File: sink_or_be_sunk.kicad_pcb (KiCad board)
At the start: 2 copper layers, 85.6 x 78.9 mm, 77 parts, among them J1 Grid_Conn_LED, J10 Grid_Conn, J11 Grid_Conn, J12 Grid_Conn, J13 Grid_Conn, J14 Grid_Conn, J15 Grid_Conn, J16 Grid_Conn, J18 Keypad_Conn, J19 Display_Conn, J2 Grid_Conn, J20 JTAG_Conn, J21 Debug_Conn, J22 Battery_Conn, J23 USB_B_Micro, J3 Grid_Conn, J4 Grid_Conn, J5 Grid_Conn, J6 Grid_Conn, J7 Grid_Conn, J8 Grid_Conn, J9 Grid_Conn, M1 Motor_DC, Q1 IRL530, Q2 Q_PMOS_DGS, Q3 2N3704, Q4 2N3704, SW1 SW_DPST, SW2 Reset_SW, U1 SN74HC151N, U2 SwitchingRegulator, U3 MCP73831-2-OT, U4 MCP608, U5 ESP32-WROOM-32, U6 CY7C65213A-28PVXI

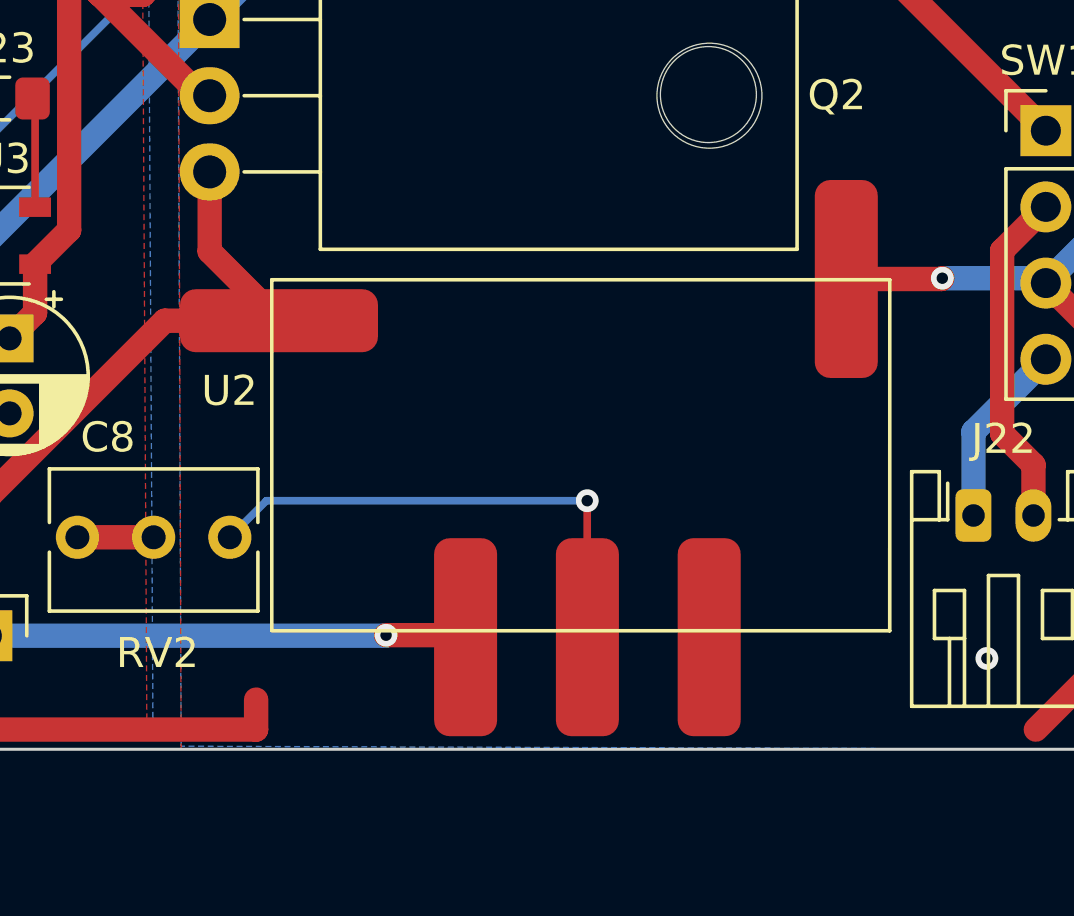
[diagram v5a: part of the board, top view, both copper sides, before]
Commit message: before switching pmos
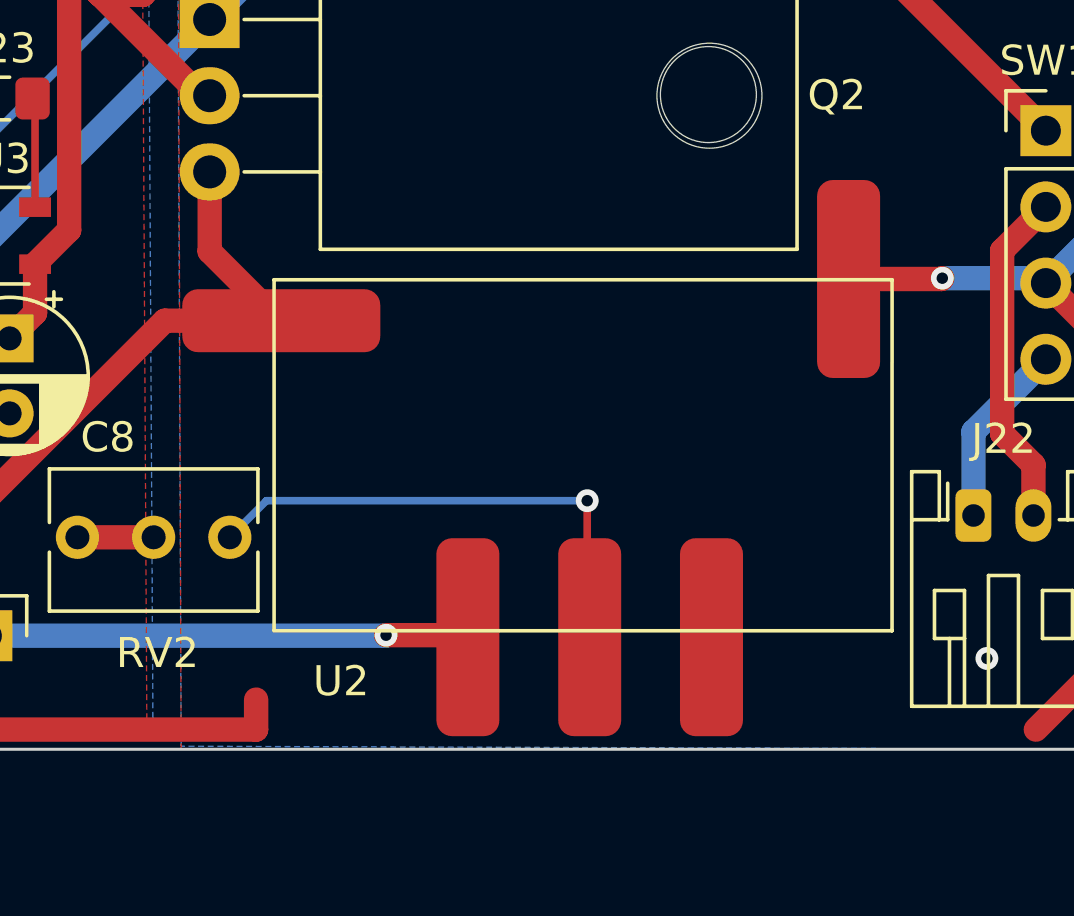
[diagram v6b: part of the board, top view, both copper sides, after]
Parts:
- moved U2 0.08 mm to (175.6, 117.7)
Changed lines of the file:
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@@
   )
   (module PCB_ESP32:SwitchingRegulator (layer F.Cu)
-    (at 175.4759 117.6782 180)
-    (fp_text reference U2 (at 11.4427 2.3622) (layer F.SilkS)
+    (at 175.5521 117.6782 180)
+    (fp_text reference U2 (at 7.7978 -7.3152) (layer F.SilkS)
       (effects (font (size 1 1) (thickness 0.15)))
     )
@@
     (fp_line (start 10.0314 -5.588) (end 10.0314 6.096) (layer F.CrtYd) (width 0.12))
     (fp_line (start 10.033 6.095) (end -10.5664 6.095) (layer F.CrtYd) (width 0.12))
+    (pad 4 smd roundrect (at -0.4886 -5.845 180) (size 2.1 6.6) (layers F.Cu F.Paste F.Mask) (roundrect_rratio 0.25)
+      (net 95 "Net-(RV2-Pad1)"))
+    (pad 3 smd roundrect (at 3.5714 -5.845 180) (size 2.1 6.6) (layers F.Cu F.Paste F.Mask) (roundrect_rratio 0.25)
+      (net 1 GND))
+    (pad 2 smd roundrect (at -9.1186 6.095 180) (size 2.1 6.6) (layers F.Cu F.Paste F.Mask) (roundrect_rratio 0.25)
+      (net 1 GND))
+    (pad 1 smd roundrect (at 9.7914 4.705 180) (size 6.6 2.1) (layers F.Cu F.Paste F.Mask) (roundrect_rratio 0.25)
+      (net 63 /Vin))
     (pad 5 smd roundrect (at -4.5486 -5.845 180) (size 2.1 6.6) (layers F.Cu F.Paste F.Mask) (roundrect_rratio 0.25)
       (net 3 +3V3))
-    (pad 1 smd roundrect (at 9.7914 4.705 180) (size 6.6 2.1) (layers F.Cu F.Paste F.Mask) (roundrect_rratio 0.25)
-      (net 63 /Vin))
-    (pad 2 smd roundrect (at -9.1186 6.095 180) (size 2.1 6.6) (layers F.Cu F.Paste F.Mask) (roundrect_rratio 0.25)
-      (net 1 GND))
-    (pad 3 smd roundrect (at 3.5714 -5.845 180) (size 2.1 6.6) (layers F.Cu F.Paste F.Mask) (roundrect_rratio 0.25)
-      (net 1 GND))
-    (pad 4 smd roundrect (at -0.4886 -5.845 180) (size 2.1 6.6) (layers F.Cu F.Paste F.Mask) (roundrect_rratio 0.25)
-      (net 95 "Net-(RV2-Pad1)"))
+    (model ${KIPRJMOD}/models/Regulator.step
+      (offset (xyz 0 0 7))
+      (scale (xyz 1 1 1))
+      (rotate (xyz 0 180 0))
+    )
   )
   (module Potentiometer_THT:Potentiometer_Bourns_3266Y_Vertical (layer F.Cu)

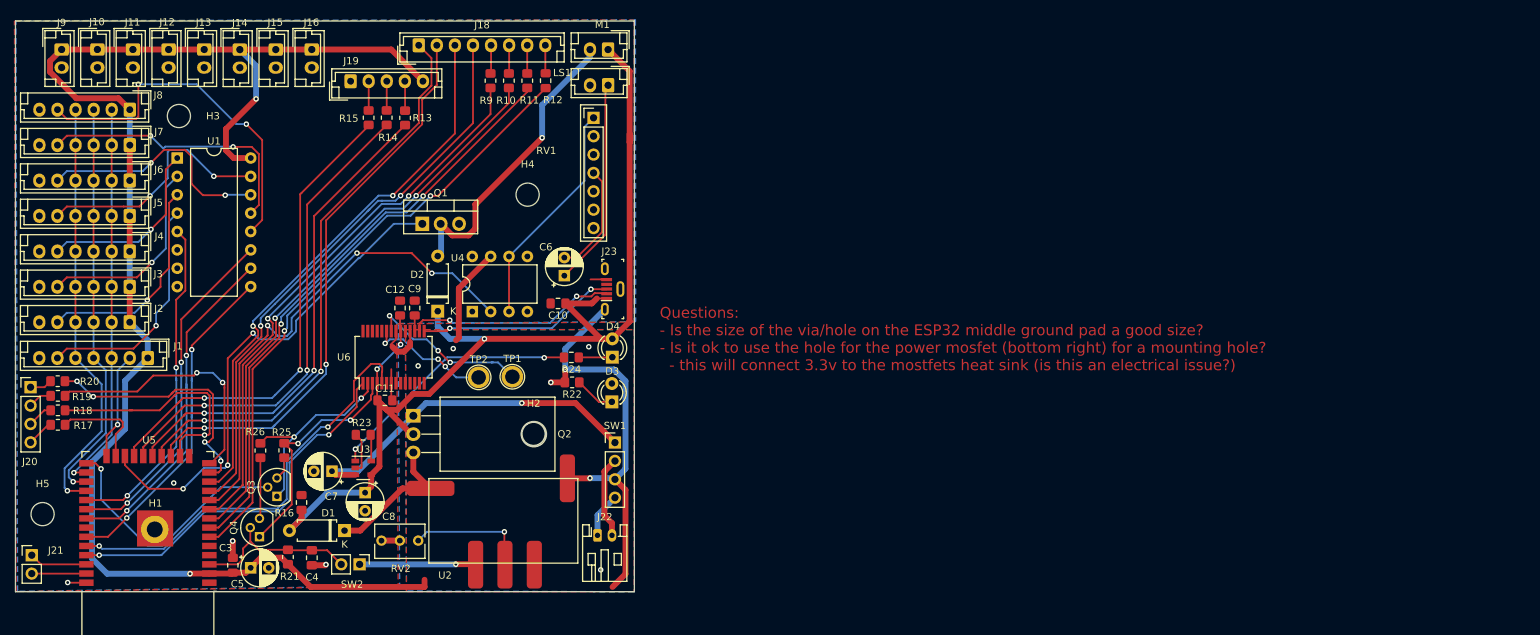
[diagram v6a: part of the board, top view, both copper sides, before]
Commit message: updated switching regulator and pmos
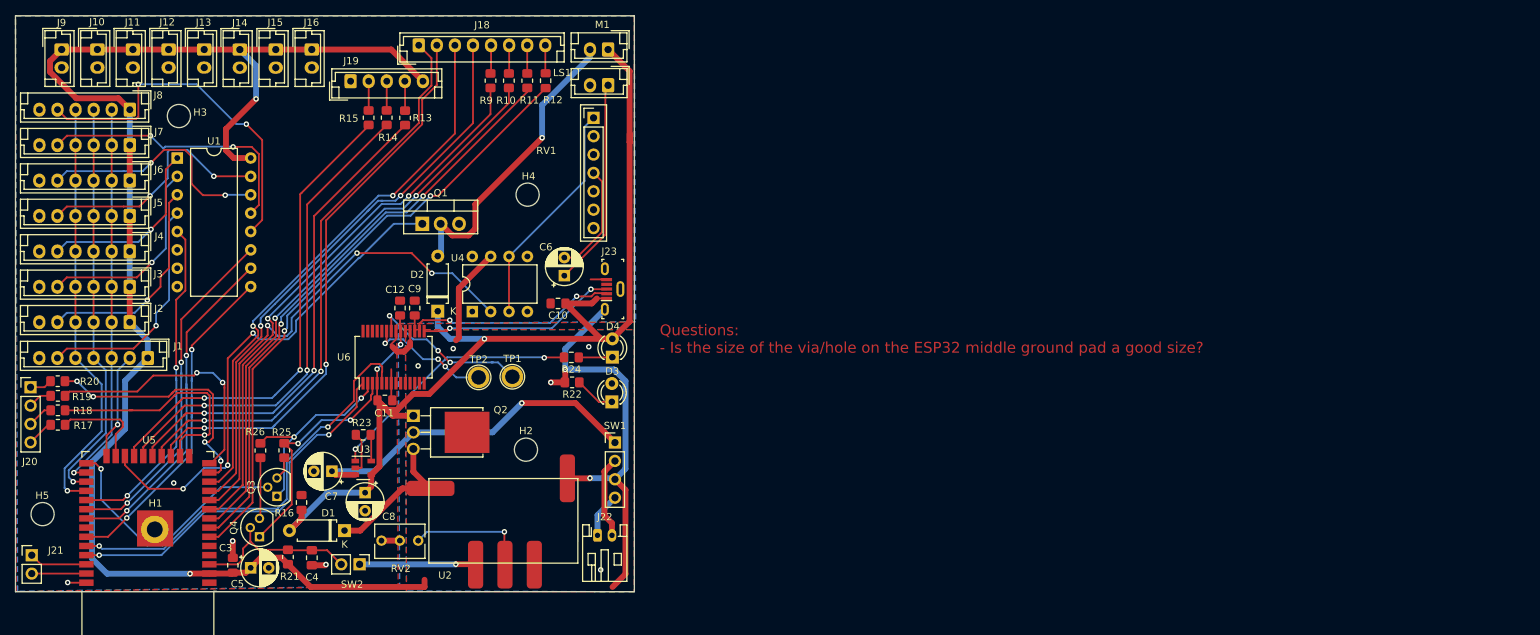
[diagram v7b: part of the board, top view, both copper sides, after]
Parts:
- Q2: value Q_PMOS_DGS -> Q_PMOS_GDS; footprint Package_TO_SOT_THT:TO-220-3_Horizontal_TabDown -> Package_TO_SOT_THT:TO-251-3-1EP_Horizontal_TabDown
- moved H2 2.43 mm to (178.9, 107.6)
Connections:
- Q2 pad 1: +BATT -> VBUS
- Q2 pad 2: VBUS -> +BATT
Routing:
- net VBUS: track 154.2 -> 153.1 mm
- net /Vin: track 20.2 -> 20.7 mm
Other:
- board size 85.6 x 78.9 mm -> 85.6 x 79.6 mm
- board text added: "Questions: - Is the size of the via/hole on the ESP32 middle ground pad a good size?"
- board text removed: "Questions: - Is the size of the via/hole on the ESP32 middle ground pad a good size? - Is it ok to use the hole for the power mosfet (bottom right) for a mounting hole? - this will connect 3.3v to the mostfets heat sink (is this an electrical issue?)"

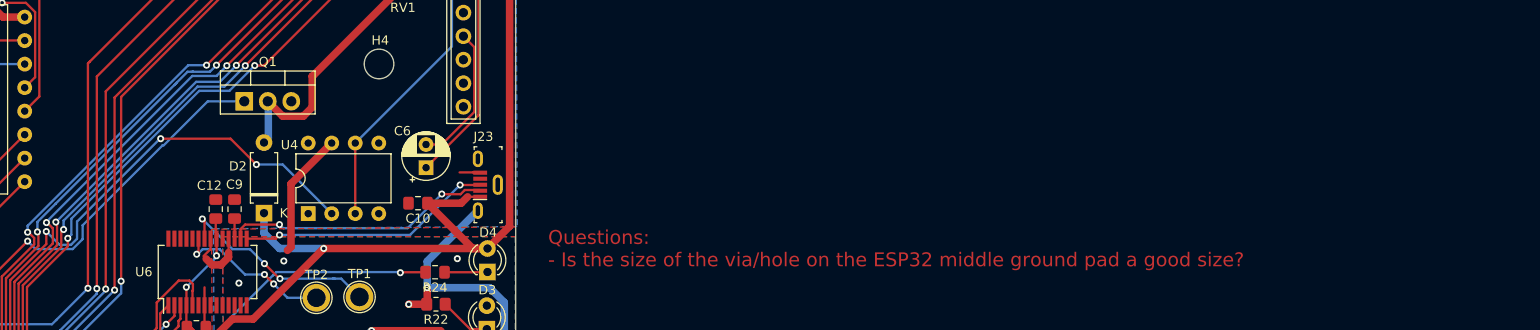
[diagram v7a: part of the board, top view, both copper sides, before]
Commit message: added logo to board
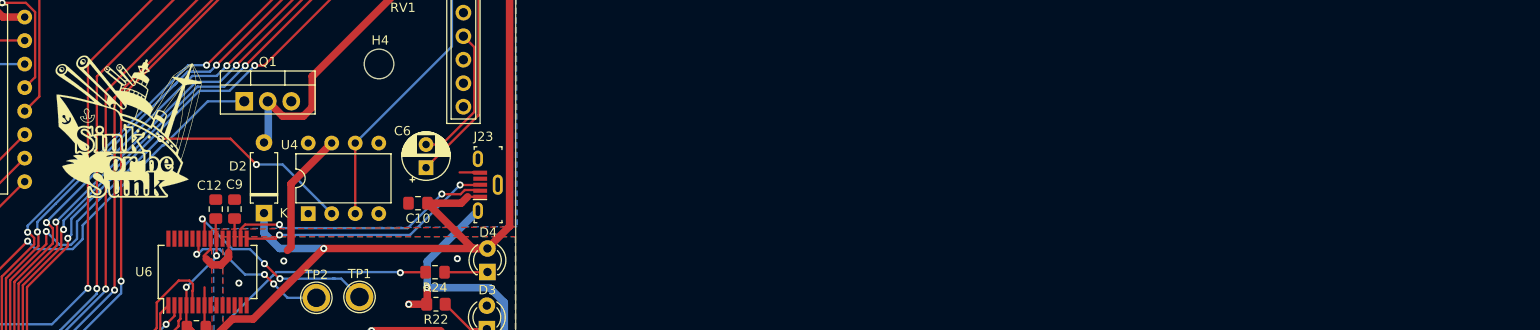
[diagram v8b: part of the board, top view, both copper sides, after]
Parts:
- added G***: LOGO, PCB_ESP32:Logo_inverted, F.Cu at (152.1, 79.0)
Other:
- board text removed: "Questions: - Is the size of the via/hole on the ESP32 middle ground pad a good size?"
